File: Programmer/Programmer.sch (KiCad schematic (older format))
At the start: 21 parts, among them J1 USB_C_Receptacle_USB2.0, J2 Prog, Q1 BC846BS, U1 AP2112K-3.3, U2 FT232RL-REEL

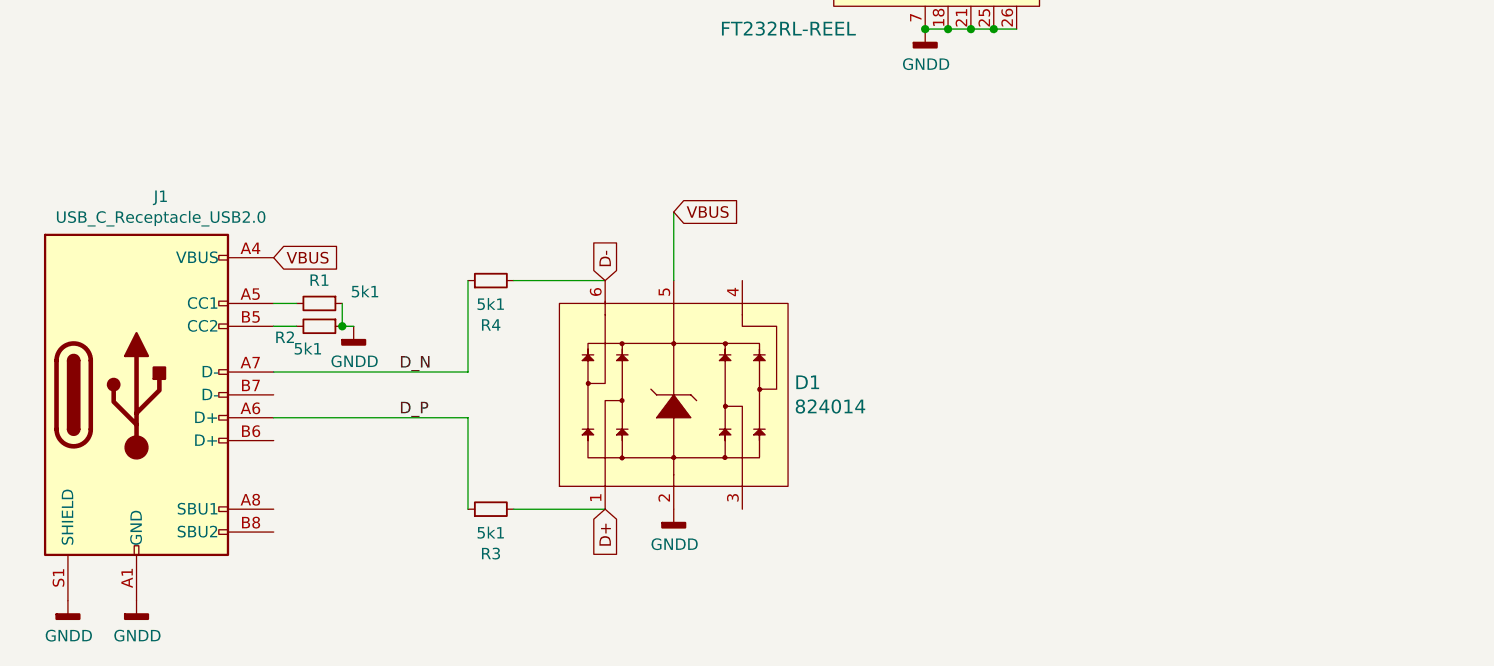
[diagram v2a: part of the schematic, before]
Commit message: Final edit
Ændret LDO , da jeg ikke kunne skaffe den anden på mouser kun i kina, hvilket jeg ikke har tid til. Rettet en bane der kom lidt for tæt og fejlede i første forsøg
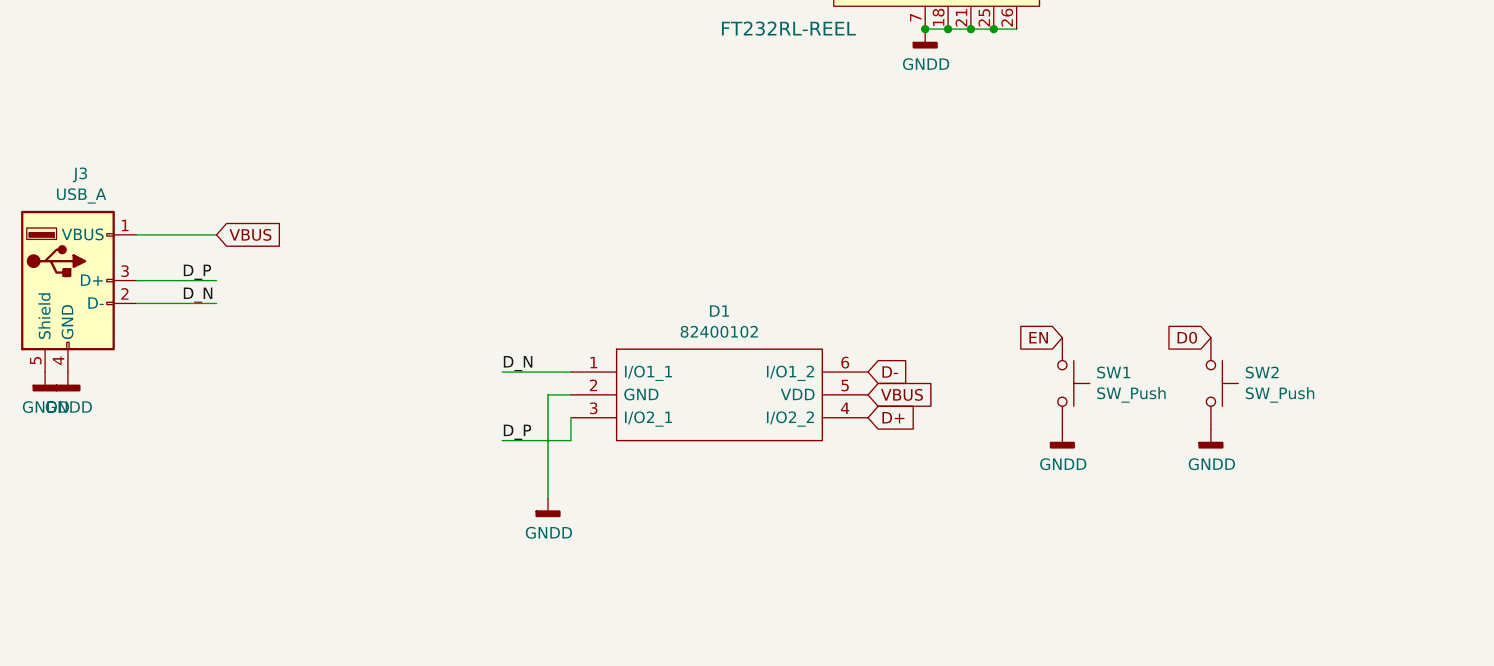
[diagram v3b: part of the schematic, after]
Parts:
- removed D1: 824014, Package_TO_SOT_SMD:SOT-23-6, symbol dk_TVS-Diodes:USBLC6-2SC6
- removed J1: USB_C_Receptacle_USB2.0, Connector_USB:USB_C_Receptacle_Amphenol_12401548E4-2A, symbol Connector:USB_C_Receptacle_USB2.0
- removed R1, R2, R3, R4: 5k1, Resistor_SMD:R_0805_2012Metric, symbol Device:R_Small
- added D1: 82400102, SOT95P280X145-6N, symbol Programmer-rescue:82400102-SamacSys_Parts
- added J3: USB_A, Connector_USB:USB_Mini-B_Wuerth_65100516121_Horizontal, symbol Connector:USB_A
- added SW1, SW2: SW_Push, Button_Switch_SMD:SW_Push_1P1T_NO_6x6mm_H9.5mm, symbol Switch:SW_Push
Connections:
- wire segments 59 -> 56
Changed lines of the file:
@@
 encoding utf-8
 Sheet 1 1
-Title ""
-Date ""
+Title "Programmer interface for ESP"
+Date "2020-08-04"
 Rev ""
 Comp ""
@@
 	3500 1050 3850 1050
 Connection ~ 3850 1050
-$Comp
-L Connector:USB_C_Receptacle_USB2.0 J1
-U 1 1 5F2A60F8
-P 1500 5300
-F 0 "J1" H 1607 6167 50  0000 C CNN
-F 1 "USB_C_Receptacle_USB2.0" H 1607 6076 50  0000 C CNN
-F 2 "Connector_USB:USB_C_Receptacle_Amphenol_12401548E4-2A" H 1650 5300 50  0001 C CNN
-F 3 "https://www.usb.org/sites/default/files/documents/usb_type-c.zip" H 1650 5300 50  0001 C CNN
-	1    1500 5300
-	1    0    0    -1
-$EndComp
-$Comp
-L power:GNDD #PWR0110
-U 1 1 5F2A860F
-P 1500 6200
-F 0 "#PWR0110" H 1500 5950 50  0001 C CNN
-F 1 "GNDD" H 1504 6045 50  0000 C CNN
-F 2 "" H 1500 6200 50  0001 C CNN
-F 3 "" H 1500 6200 50  0001 C CNN
-	1    1500 6200
-	1    0    0    -1
-$EndComp
 Text GLabel 3500 1050 0    50   Input ~ 0
 VBUS
-Text GLabel 2100 4700 2    50   Input ~ 0
-VBUS
-$Comp
-L Device:R_Small R3
-U 1 1 5F2A90CC
-P 3050 5800
-F 0 "R3" V 2854 5800 50  0000 C CNN
-F 1 "5k1" V 2945 5800 50  0000 C CNN
-F 2 "Resistor_SMD:R_0805_2012Metric" H 3050 5800 50  0001 C CNN
-F 3 "~" H 3050 5800 50  0001 C CNN
-	1    3050 5800
-	0    -1   -1   0
-$EndComp
-$Comp
-L Device:R_Small R4
-U 1 1 5F2A9F6E
-P 3050 4800
-F 0 "R4" V 2854 4800 50  0000 C CNN
-F 1 "5k1" V 2945 4800 50  0000 C CNN
-F 2 "Resistor_SMD:R_0805_2012Metric" H 3050 4800 50  0001 C CNN
-F 3 "~" H 3050 4800 50  0001 C CNN
-	1    3050 4800
-	0    -1   -1   0
-$EndComp
-$Comp
-L Device:R_Small R1
-U 1 1 5F2AC5D0
-P 2300 4900
-F 0 "R1" V 2200 4900 50  0000 C CNN
-F 1 "5k1" V 2250 5100 50  0000 C CNN
-F 2 "Resistor_SMD:R_0805_2012Metric" H 2300 4900 50  0001 C CNN
-F 3 "~" H 2300 4900 50  0001 C CNN
-	1    2300 4900
-	0    1    1    0
-$EndComp
-$Comp
-L Device:R_Small R2
-U 1 1 5F2ACF8D
-P 2300 5000
-F 0 "R2" V 2350 4850 50  0000 C CNN
-F 1 "5k1" V 2400 4950 50  0000 C CNN
-F 2 "Resistor_SMD:R_0805_2012Metric" H 2300 5000 50  0001 C CNN
-F 3 "~" H 2300 5000 50  0001 C CNN
-	1    2300 5000
-	0    1    1    0
-$EndComp
-Wire Wire Line
-	2200 4900 2100 4900
-Wire Wire Line
-	2200 5000 2100 5000
-Wire Wire Line
-	2400 4900 2400 5000
-$Comp
-L power:GNDD #PWR0111
-U 1 1 5F2B1DF3
-P 2450 5000
-F 0 "#PWR0111" H 2450 4750 50  0001 C CNN
-F 1 "GNDD" H 2454 4845 50  0000 C CNN
-F 2 "" H 2450 5000 50  0001 C CNN
-F 3 "" H 2450 5000 50  0001 C CNN
-	1    2450 5000
-	1    0    0    -1
-$EndComp
-Wire Wire Line
-	2450 5000 2400 5000
-Connection ~ 2400 5000
-Text GLabel 3550 5800 3    50   Input ~ 0
+Text GLabel 4700 5400 2    50   Input ~ 0
 D+
-Text GLabel 3550 4800 1    50   Input ~ 0
+Text GLabel 4700 5200 2    50   Input ~ 0
 D-
 Text GLabel 4100 2300 0    50   Input ~ 0
@@
 D+
 $Comp
-L dk_TVS-Diodes:USBLC6-2SC6 D1
-U 1 1 5F282DC2
-P 3850 5300
-F 0 "D1" V 3903 4772 60  0000 R CNN
-F 1 "824014" V 3797 4772 60  0000 R CNN
-F 2 "Package_TO_SOT_SMD:SOT-23-6" H 4050 5500 60  0001 L CNN
-F 3 "http://www.st.com/content/ccc/resource/technical/document/datasheet/06/1d/48/9c/6c/20/4a/b2/CD00050750.pdf/files/CD00050750.pdf/jcr:content/translations/en.CD00050750.pdf" H 4050 5600 60  0001 L CNN
-F 4 "497-5235-1-ND" H 4050 5700 60  0001 L CNN "Digi-Key_PN"
-F 5 "USBLC6-2SC6" H 4050 5800 60  0001 L CNN "MPN"
-F 6 "Circuit Protection" H 4050 5900 60  0001 L CNN "Category"
-F 7 "TVS - Diodes" H 4050 6000 60  0001 L CNN "Family"
-F 8 "http://www.st.com/content/ccc/resource/technical/document/datasheet/06/1d/48/9c/6c/20/4a/b2/CD00050750.pdf/files/CD00050750.pdf/jcr:content/translations/en.CD00050750.pdf" H 4050 6100 60  0001 L CNN "DK_Datasheet_Link"
-F 9 "/product-detail/en/stmicroelectronics/USBLC6-2SC6/497-5235-1-ND/1121688" H 4050 6200 60  0001 L CNN "DK_Detail_Page"
-F 10 "TVS DIODE 5.25V 17V SOT23-6" H 4050 6300 60  0001 L CNN "Description"
-F 11 "STMicroelectronics" H 4050 6400 60  0001 L CNN "Manufacturer"
-F 12 "Active" H 4050 6500 60  0001 L CNN "Status"
-	1    3850 5300
-	0    -1   -1   0
-$EndComp
-Wire Wire Line
-	3550 5800 3150 5800
-Wire Wire Line
-	3550 4800 3150 4800
-Wire Wire Line
-	2100 5400 2950 5400
-Wire Wire Line
-	2100 5200 2950 5200
-$Comp
 L power:GNDD #PWR0112
 U 1 1 5F29BCC2
-P 3850 5800
-F 0 "#PWR0112" H 3850 5550 50  0001 C CNN
-F 1 "GNDD" H 3854 5645 50  0000 C CNN
-F 2 "" H 3850 5800 50  0001 C CNN
-F 3 "" H 3850 5800 50  0001 C CNN
-	1    3850 5800
-	1    0    0    -1
-$EndComp
-Text GLabel 3850 4500 2    50   Input ~ 0
+P 3300 5750
+F 0 "#PWR0112" H 3300 5500 50  0001 C CNN
+F 1 "GNDD" H 3304 5595 50  0000 C CNN
+F 2 "" H 3300 5750 50  0001 C CNN
+F 3 "" H 3300 5750 50  0001 C CNN
+	1    3300 5750
+	1    0    0    -1
+$EndComp
+Text GLabel 4700 5300 2    50   Input ~ 0
 VBUS
-Wire Wire Line
-	3850 4800 3850 4500
-Text Label 2650 5200 0    50   ~ 0
+Text Label 3100 5200 0    50   ~ 0
 D_N
-Text Label 2650 5400 0    50   ~ 0
+Text Label 3100 5500 0    50   ~ 0
 D_P
-Wire Wire Line
-	2950 4800 2950 5200
-Wire Wire Line
-	2950 5400 2950 5800
 $Comp
 L power:VCC #PWR0107
@@
 Wire Wire Line
 	4300 2400 4300 2050
-$Comp
-L power:GNDD #PWR0115
-U 1 1 5F296ACA
-P 1200 6200
-F 0 "#PWR0115" H 1200 5950 50  0001 C CNN
-F 1 "GNDD" H 1204 6045 50  0000 C CNN
-F 2 "" H 1200 6200 50  0001 C CNN
-F 3 "" H 1200 6200 50  0001 C CNN
-	1    1200 6200
-	1    0    0    -1
-$EndComp
 $Comp
 L Device:LED D2
@@
 	3400 3250 3200 3250
 $Comp
-L power:VCC #PWR?
+L power:VCC #PWR0116
 U 1 1 5F2A9A67
 P 3200 3250
-F 0 "#PWR?" H 3200 3100 50  0001 C CNN
+F 0 "#PWR0116" H 3200 3100 50  0001 C CNN
 F 1 "VCC" H 3215 3423 50  0000 C CNN
 F 2 "" H 3200 3250 50  0001 C CNN
@@
 $EndComp
 Connection ~ 3200 3250
+$Comp
+L Switch:SW_Push SW1
+U 1 1 5F294DD1
+P 5550 5250
+F 0 "SW1" V 5504 5398 50  0000 L CNN
+F 1 "SW_Push" V 5595 5398 50  0000 L CNN
+F 2 "Button_Switch_SMD:SW_Push_1P1T_NO_6x6mm_H9.5mm" H 5550 5450 50  0001 C CNN
+F 3 "~" H 5550 5450 50  0001 C CNN
+	1    5550 5250
+	0    1    1    0
+$EndComp
+$Comp
+L power:GNDD #PWR0117
+U 1 1 5F295D17
+P 5550 5450
+F 0 "#PWR0117" H 5550 5200 50  0001 C CNN
+F 1 "GNDD" H 5554 5295 50  0000 C CNN
+F 2 "" H 5550 5450 50  0001 C CNN
+F 3 "" H 5550 5450 50  0001 C CNN
+	1    5550 5450
+	1    0    0    -1
+$EndComp
+Text GLabel 5550 5050 0    50   Input ~ 0
+EN
+$Comp
+L Switch:SW_Push SW2
+U 1 1 5F294330
+P 6200 5250
+F 0 "SW2" V 6154 5398 50  0000 L CNN
+F 1 "SW_Push" V 6245 5398 50  0000 L CNN
+F 2 "Button_Switch_SMD:SW_Push_1P1T_NO_6x6mm_H9.5mm" H 6200 5450 50  0001 C CNN
+F 3 "~" H 6200 5450 50  0001 C CNN
+	1    6200 5250
+	0    1    1    0
+$EndComp
+$Comp
+L power:GNDD #PWR0118
+U 1 1 5F294336
+P 6200 5450
+F 0 "#PWR0118" H 6200 5200 50  0001 C CNN
+F 1 "GNDD" H 6204 5295 50  0000 C CNN
+F 2 "" H 6200 5450 50  0001 C CNN
+F 3 "" H 6200 5450 50  0001 C CNN
+	1    6200 5450
+	1    0    0    -1
+$EndComp
+Text GLabel 6200 5050 0    50   Input ~ 0
+D0
+$Comp
+L Connector:USB_A J3
+U 1 1 5F354476
+P 1200 4800
+F 0 "J3" H 1257 5267 50  0000 C CNN
+F 1 "USB_A" H 1257 5176 50  0000 C CNN
+F 2 "Connector_USB:USB_Mini-B_Wuerth_65100516121_Horizontal" H 1350 4750 50  0001 C CNN
+F 3 " ~" H 1350 4750 50  0001 C CNN
+	1    1200 4800
+	1    0    0    -1
+$EndComp
+$Comp
+L power:GNDD #PWR0119
+U 1 1 5F355B3F
+P 1200 5200
+F 0 "#PWR0119" H 1200 4950 50  0001 C CNN
+F 1 "GNDD" H 1204 5045 50  0000 C CNN
+F 2 "" H 1200 5200 50  0001 C CNN
+F 3 "" H 1200 5200 50  0001 C CNN
+	1    1200 5200
+	1    0    0    -1
+$EndComp
+$Comp
+L power:GNDD #PWR0120
+U 1 1 5F35609A
+P 1100 5200
+F 0 "#PWR0120" H 1100 4950 50  0001 C CNN
+F 1 "GNDD" H 1104 5045 50  0000 C CNN
+F 2 "" H 1100 5200 50  0001 C CNN
+F 3 "" H 1100 5200 50  0001 C CNN
+	1    1100 5200
+	1    0    0    -1
+$EndComp
+Wire Wire Line
+	1500 4600 1850 4600
+Wire Wire Line
+	1500 4800 1850 4800
+Wire Wire Line
+	1500 4900 1850 4900
+Text Label 1700 4900 0    50   ~ 0
+D_N
+Text Label 1700 4800 0    50   ~ 0
+D_P
+Text GLabel 1850 4600 2    50   Input ~ 0
+VBUS
+$Comp
+L Programmer-rescue:82400102-SamacSys_Parts D1
+U 1 1 5F36845F
+P 3400 5200
+F 0 "D1" H 4050 5465 50  0000 C CNN
+F 1 "82400102" H 4050 5374 50  0000 C CNN
+F 2 "SOT95P280X145-6N" H 4550 5300 50  0001 L CNN
+F 3 "http://katalog.we-online.de/pbs/datasheet/82400102.pdf" H 4550 5200 50  0001 L CNN
+F 4 "TVS Diode Array WE-TVS 2-Ch+VDD 5V SOT23 Wurth Elektronik 82400102, Uni-Directional TVS Diode Array Array, 7.7V, 6-Pin SOT-23" H 4550 5100 50  0001 L CNN "Description"
+F 5 "1.45" H 4550 5000 50  0001 L CNN "Height"
+F 6 "Wurth Elektronik" H 4550 4900 50  0001 L CNN "Manufacturer_Name"
+F 7 "82400102" H 4550 4800 50  0001 L CNN "Manufacturer_Part_Number"
+F 8 "82400102" H 4550 4700 50  0001 L CNN "Arrow Part Number"
+F 9 "" H 4550 4600 50  0001 L CNN "Arrow Price/Stock"
+F 10 "710-82400102" H 4550 4500 50  0001 L CNN "Mouser Part Number"
+F 11 "https://www.mouser.co.uk/ProductDetail/Wurth-Elektronik/82400102?qs=Wn16VcyqZWq4x2NXBP4V%252Bw%3D%3D" H 4550 4400 50  0001 L CNN "Mouser Price/Stock"
+	1    3400 5200
+	1    0    0    -1
+$EndComp
+Wire Wire Line
+	3400 5400 3400 5500
+Wire Wire Line
+	3400 5500 3100 5500
+Wire Wire Line
+	3100 5200 3400 5200
+Wire Wire Line
+	3400 5300 3300 5300
+Wire Wire Line
+	3300 5300 3300 5750
 $EndSCHEMATC
